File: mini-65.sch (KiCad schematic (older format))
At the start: 170 parts, among them J1 TYPE-C-31-M12_13_EDITED, J2 AVR-ISP-6, SW1 SW_Push, U1 ATmega32U4-AU, U2 USBLC6-2SC6, Y1 Crystal_GND24_Small

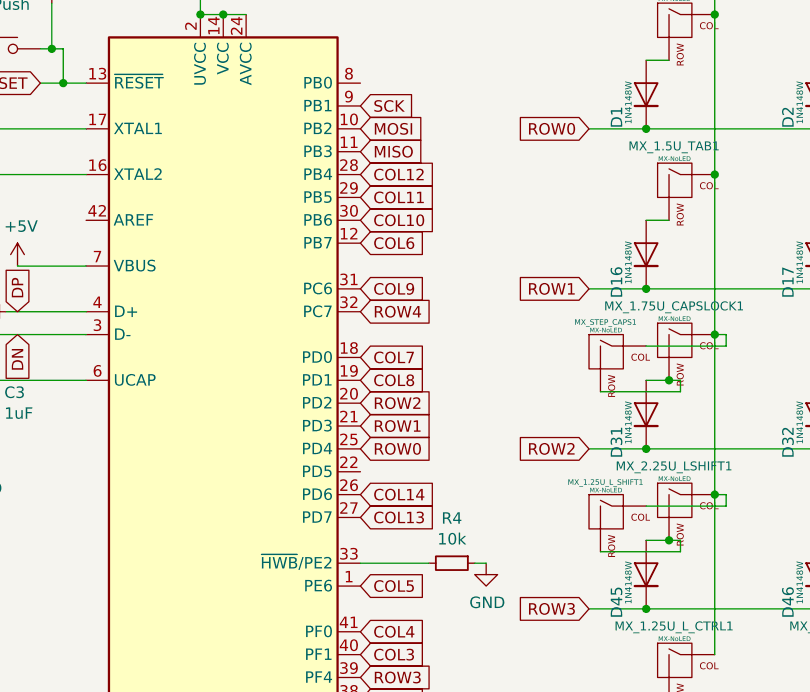
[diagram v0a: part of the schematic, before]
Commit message: All col/rows routed, ground screw pads extended
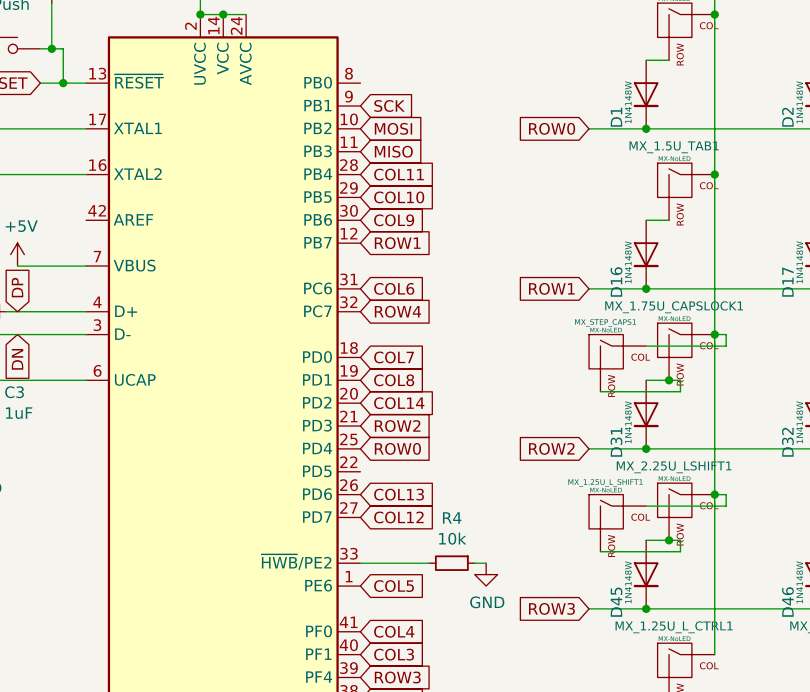
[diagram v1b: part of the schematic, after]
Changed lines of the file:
@@
 	1    0    0    -1
 $EndComp
-Text GLabel 3150 2950 2    50   Input ~ 0
-ROW0
-Text GLabel 3150 2850 2    50   Input ~ 0
-ROW1
-Text GLabel 3150 2750 2    50   Input ~ 0
-ROW2
 Wire Wire Line
 	2450 4650 2100 4650
@@
 	1    0    0    -1
 $EndComp
-Text GLabel 3150 3950 2    50   Input ~ 0
-ROW3
-Text GLabel 3150 2350 2    50   Input ~ 0
-ROW4
-Text GLabel 3150 4050 2    50   Input ~ 0
-COL0
-Text GLabel 3150 4150 2    50   Input ~ 0
-COL1
-Text GLabel 3150 4250 2    50   Input ~ 0
-COL2
-Text GLabel 3150 3850 2    50   Input ~ 0
-COL3
-Text GLabel 3150 3750 2    50   Input ~ 0
-COL4
-Text GLabel 3150 3550 2    50   Input ~ 0
-COL5
-Text GLabel 3150 2050 2    50   Input ~ 0
-COL6
-Text GLabel 3150 2550 2    50   Input ~ 0
-COL7
-Text GLabel 3150 2650 2    50   Input ~ 0
-COL8
-Text GLabel 3150 2250 2    50   Input ~ 0
-COL9
-Text GLabel 3150 1950 2    50   Input ~ 0
-COL10
-Text GLabel 3150 1850 2    50   Input ~ 0
-COL11
-Text GLabel 3150 1750 2    50   Input ~ 0
-COL12
-Text GLabel 3150 3150 2    50   Input ~ 0
-COL14
-Text GLabel 3150 3250 2    50   Input ~ 0
-COL13
 $Comp
 L Power_Protection:USBLC6-2SC6 U2
@@
 Wire Wire Line
 	8550 6350 8550 6400
+Text GLabel 3150 2950 2    50   Input ~ 0
+ROW0
+Text GLabel 3150 2050 2    50   Input ~ 0
+ROW1
+Text GLabel 3150 2850 2    50   Input ~ 0
+ROW2
+Text GLabel 3150 2750 2    50   Input ~ 0
+COL14
+Text GLabel 3150 3150 2    50   Input ~ 0
+COL13
+Text GLabel 3150 3250 2    50   Input ~ 0
+COL12
+Text GLabel 3150 1750 2    50   Input ~ 0
+COL11
+Text GLabel 3150 1850 2    50   Input ~ 0
+COL10
+Text GLabel 3150 1950 2    50   Input ~ 0
+COL9
+Text GLabel 3150 2650 2    50   Input ~ 0
+COL8
+Text GLabel 3150 2550 2    50   Input ~ 0
+COL7
+Text GLabel 3150 2250 2    50   Input ~ 0
+COL6
+Text GLabel 3150 3550 2    50   Input ~ 0
+COL5
+Text GLabel 3150 3750 2    50   Input ~ 0
+COL4
+Text GLabel 3150 3850 2    50   Input ~ 0
+COL3
+Text GLabel 3150 3950 2    50   Input ~ 0
+ROW3
+Text GLabel 3150 4050 2    50   Input ~ 0
+COL0
+Text GLabel 3150 4150 2    50   Input ~ 0
+COL1
+Text GLabel 3150 4250 2    50   Input ~ 0
+COL2
+Text GLabel 3150 2350 2    50   Input ~ 0
+ROW4
 $EndSCHEMATC

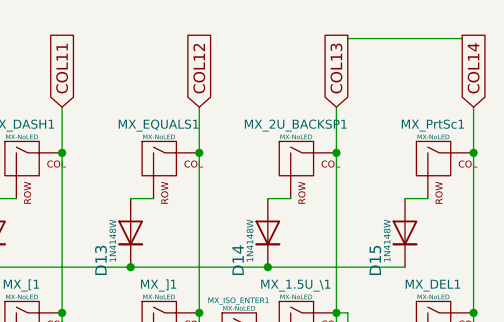
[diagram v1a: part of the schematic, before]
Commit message: Changed position of C5
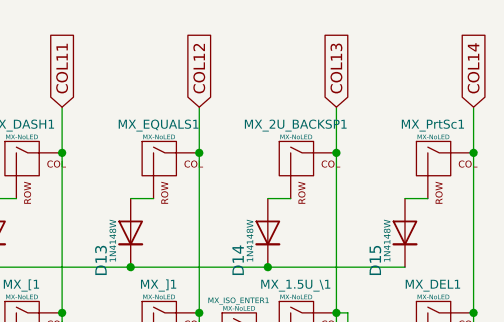
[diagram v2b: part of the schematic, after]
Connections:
- wire segments 325 -> 324
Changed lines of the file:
@@
 Connection ~ 12800 1050
-Wire Wire Line
-	12850 550  13350 550
 Wire Wire Line
 	11300 4350 11900 4350

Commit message: Changed diode positions and misc. ground changes
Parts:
- MX_6.25U_SPACE1: footprint MX_Only:MXOnly-6.25U-NoLED -> MX_Only:MXOnly-6.25U-ReversedStabilizers-NoLED
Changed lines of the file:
@@
 F 0 "MX_6.25U_SPACE1" H 8422 4074 39  0000 C CNN
 F 1 "MX-NoLED" H 8424 4019 20  0000 C CNN
-F 2 "MX_Only:MXOnly-6.25U-NoLED" H 7825 3875 60  0001 C CNN
+F 2 "MX_Only:MXOnly-6.25U-ReversedStabilizers-NoLED" H 7825 3875 60  0001 C CNN
 F 3 "" H 7825 3875 60  0001 C CNN
 	1    8450 3900

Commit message: Tweaked the MX footprints to include plated holes
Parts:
- MX_'1, MX_,1, MX_.1, MX_/1, MX_0, MX_1, MX_2, MX_3, MX_4, MX_5, MX_6, MX_7, MX_8, MX_9, MX_;1, MX_A1, MX_ARR_D1, MX_ARR_L1, MX_ARR_R1, MX_ARR_U1, MX_B1, MX_C1, MX_D1, MX_DASH1, MX_DEL1, MX_E1, MX_EQUALS1, MX_ESC1, MX_F1, MX_FN1, MX_G1, MX_H1, MX_I1, MX_INS1, MX_ISO_\1, MX_J1, MX_K1, MX_L1, MX_L_ALT1, MX_L_BSLASH1, MX_M1, MX_N1, MX_O1, MX_P1, MX_PrtSc1, MX_Q1, MX_R1, MX_R_CTRL1, MX_S1, MX_STEP_CAPS1, MX_T1, MX_TEMP1, MX_U1, MX_V1, MX_W1, MX_X1, MX_Y1, MX_Z1, MX_[1, MX_]1: footprint MX_Only:MXOnly-1U-NoLED -> mini-MX-Tweaks:MXOnly-1U-NoLED_tweak
- MX_1.25U_FN1, MX_1.25U_L_ALT1, MX_1.25U_L_CTRL1, MX_1.25U_L_SHIFT1, MX_1.25U_L_WIN1, MX_1.25U_R_CTRL1: footprint MX_Only:MXOnly-1.25U-NoLED -> mini-MX-Tweaks:MXOnly-1.25U-NoLED_tweak
- MX_1.5U_TAB1, MX_1.5U_\1: footprint MX_Only:MXOnly-1.5U-NoLED -> mini-MX-Tweaks:MXOnly-1.5U-NoLED_tweak
- MX_1.75U_CAPSLOCK1, MX_1.75U__RSHIFT1: footprint MX_Only:MXOnly-1.75U-NoLED -> mini-MX-Tweaks:MXOnly-1.75U-NoLED_tweak
- MX_2.25U_ENTER1, MX_2.25U_LSHIFT1: footprint MX_Only:MXOnly-2.25U-NoLED -> mini-MX-Tweaks:MXOnly-2.25U-NoLED_tweak
- MX_2U_BACKSP1: footprint MX_Only:MXOnly-2U-NoLED -> mini-MX-Tweaks:MXOnly-2U-NoLED_tweak
- MX_6.25U_SPACE1: footprint MX_Only:MXOnly-6.25U-ReversedStabilizers-NoLED -> mini-MX-Tweaks:MXOnly-6.25U-ReversedStabilizers-NoLED_tweak
- MX_ISO_ENTER1: footprint MX_Only:MXOnly-ISO-ROTATED-ReversedStabilizers-NoLED -> mini-MX-Tweaks:MXOnly-ISO-ROTATED-ReversedStabilizers-NoLED_tweak

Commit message: Updated PCB to tweaked footprints
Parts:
- D1, D10, D11, D12, D13, D14, D15, D16, D17, D18, D19, D2, D20, D21, D22, D23, D24, D25, D26, D27, D28, D29, D3, D30, D31, D32, D33, D34, D35, D36, D37, D38, D39, D4, D40, D41, D42, D43, D44, D45, D46, D47, D48, D49, D5, D50, D51, D52, D53, D54, D55, D56, D57, D58, D59, D6, D60, D61, D62, D63, D64, D65, D66, D67, D68, D69, D7, D8, D9: footprint canadian_footprints:D_SOD123_axial-dual -> mini-general-tweaks:D_SOD123_axial-dual
- H0, H1, H2, H3, H4, H5: footprint MountingHole:MountingHole_2.2mm_M2_Pad -> mini-general-tweaks:MountingHole_2.2mm_M2_Pad_tweaked
- J2: footprint Connector_PinHeader_2.54mm:PinHeader_2x03_P2.54mm_Vertical -> mini-general-tweaks:PinHeader_2x03_P2.54mm_Vertical_ICSP
- U1: footprint Package_QFP:TQFP-44_10x10mm_P0.8mm -> mini-general-tweaks:TQFP-44_10x10mm_P0.8mm_ATmega32U4
- U2: footprint Package_TO_SOT_SMD:SOT-23-6 -> mini-general-tweaks:SOT-23-6_tweaked

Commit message: Restructured USB area, general silkscreen tweaks
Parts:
- J1: footprint Type-C:HRO-TYPE-C-31-M-12-HandSoldering -> mini-general-tweaks:HRO-TYPE-C-31-M-12-HandSoldering_tweaked
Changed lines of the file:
@@
 F 0 "J1" H 4057 7867 50  0000 C CNN
 F 1 "TYPE-C-31-M12_13_EDITED" H 4057 7776 50  0000 C CNN
-F 2 "Type-C:HRO-TYPE-C-31-M-12-HandSoldering" V 3450 6500 50  0001 C CNN
+F 2 "mini-general-tweaks:HRO-TYPE-C-31-M-12-HandSoldering_tweaked" V 3450 6500 50  0001 C CNN
 F 3 "" H 4150 6500 50  0001 C CNN
 	1    3950 6450

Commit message: misc changes, including ICSP silkscreen
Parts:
- J2: footprint mini-general-tweaks:PinHeader_2x03_P2.54mm_Vertical_ICSP -> mini-general-tweaks:ICSP_2.54mm_LAYOUT
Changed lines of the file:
@@
 F 0 "J2" H 921 6596 50  0000 R CNN
 F 1 "AVR-ISP-6" H 921 6505 50  0000 R CNN
-F 2 "mini-general-tweaks:PinHeader_2x03_P2.54mm_Vertical_ICSP" V 950 6550 50  0001 C CNN
+F 2 "mini-general-tweaks:ICSP_2.54mm_LAYOUT" V 950 6550 50  0001 C CNN
 F 3 " ~" H -75 5950 50  0001 C CNN
 	1    1200 6500
@@
 	1    0    0    -1
 $EndComp
-Connection ~ 2450 1050
 Wire Wire Line
 	4200 2700 4550 2700
@@
 Wire Wire Line
 	8550 6350 8550 6400
-Text GLabel 3150 2950 2    50   Input ~ 0
-ROW0
-Text GLabel 3150 2050 2    50   Input ~ 0
-ROW1
-Text GLabel 3150 2850 2    50   Input ~ 0
-ROW2
-Text GLabel 3150 2750 2    50   Input ~ 0
-COL14
-Text GLabel 3150 3150 2    50   Input ~ 0
-COL13
-Text GLabel 3150 3250 2    50   Input ~ 0
-COL12
-Text GLabel 3150 1750 2    50   Input ~ 0
-COL11
-Text GLabel 3150 1850 2    50   Input ~ 0
-COL10
-Text GLabel 3150 1950 2    50   Input ~ 0
-COL9
-Text GLabel 3150 2650 2    50   Input ~ 0
-COL8
-Text GLabel 3150 2550 2    50   Input ~ 0
-COL7
-Text GLabel 3150 2250 2    50   Input ~ 0
-COL6
-Text GLabel 3150 2350 2    50   Input ~ 0
-ROW4
 Connection ~ 5450 3150
 Connection ~ 6500 3650
-Connection ~ 2550 1050
-Wire Wire Line
-	2650 1050 2550 1050
-Wire Wire Line
-	2550 1050 2450 1050
 Connection ~ 8300 4350
-Text GLabel 3150 4250 2    50   Input ~ 0
-COL2
-Text GLabel 3150 4150 2    50   Input ~ 0
-COL1
-Text GLabel 3150 4050 2    50   Input ~ 0
-COL0
-Text GLabel 3150 3950 2    50   Input ~ 0
-ROW3
-Text GLabel 3150 3850 2    50   Input ~ 0
-COL3
-Text GLabel 3150 3750 2    50   Input ~ 0
-COL4
-Text GLabel 3150 3550 2    50   Input ~ 0
-COL5
 Wire Wire Line
 	5450 3150 5450 3850
@@
 	5900 3650 6500 3650
 Connection ~ 4400 3650
-$Comp
-L MCU_Microchip_ATmega:ATmega32U4-AU U1
-U 1 1 5F16167A
-P 2550 2850
-F 0 "U1" H 2550 961 50  0000 C CNN
-F 1 "ATmega32U4-AU" H 2550 870 50  0000 C CNN
-F 2 "mini-general-tweaks:TQFP-44_10x10mm_P0.8mm_ATmega32U4" H 2550 2850 50  0001 C CIN
-F 3 "http://ww1.microchip.com/downloads/en/DeviceDoc/Atmel-7766-8-bit-AVR-ATmega16U4-32U4_Datasheet.pdf" H 2550 2850 50  0001 C CNN
-	1    2550 2850
-	1    0    0    -1
-$EndComp
 Wire Wire Line
 	3150 3450 3450 3450
-Connection ~ 2450 4650
-Wire Wire Line
-	2550 4650 2450 4650
-Wire Wire Line
-	2450 4650 2100 4650
 Connection ~ 5150 3650
 Wire Wire Line
@@
 	1    0    0    -1
 $EndComp
+Text GLabel 3150 3550 2    50   Input ~ 0
+COL5
+Text GLabel 3150 3750 2    50   Input ~ 0
+COL4
+Text GLabel 3150 3850 2    50   Input ~ 0
+COL3
+Text GLabel 3150 1850 2    50   Input ~ 0
+ROW3
+Text GLabel 3150 4050 2    50   Input ~ 0
+COL1
+Text GLabel 3150 4150 2    50   Input ~ 0
+COL0
+Text GLabel 3150 3950 2    50   Input ~ 0
+COL2
+Wire Wire Line
+	2450 4650 2100 4650
+Wire Wire Line
+	2550 4650 2450 4650
+Connection ~ 2450 4650
+Wire Wire Line
+	2550 1050 2450 1050
+Wire Wire Line
+	2650 1050 2550 1050
+Connection ~ 2550 1050
+Connection ~ 2450 1050
+Text GLabel 3150 4250 2    50   Input ~ 0
+ROW0
+Text GLabel 3150 2050 2    50   Input ~ 0
+ROW1
+Text GLabel 3150 1950 2    50   Input ~ 0
+ROW2
+Text GLabel 3150 2250 2    50   Input ~ 0
+COL14
+Text GLabel 3150 3250 2    50   Input ~ 0
+COL12
+Text GLabel 3150 3150 2    50   Input ~ 0
+COL11
+Text GLabel 3150 2950 2    50   Input ~ 0
+COL10
+Text GLabel 3150 2850 2    50   Input ~ 0
+COL9
+Text GLabel 3150 2750 2    50   Input ~ 0
+COL8
+Text GLabel 3150 2650 2    50   Input ~ 0
+COL7
+Text GLabel 3150 2550 2    50   Input ~ 0
+COL6
+Text GLabel 3150 2350 2    50   Input ~ 0
+ROW4
+$Comp
+L MCU_Microchip_ATmega:ATmega32U4-AU U1
+U 1 1 5F16167A
+P 2550 2850
+F 0 "U1" H 2550 961 50  0000 C CNN
+F 1 "ATmega32U4-AU" H 2550 870 50  0000 C CNN
+F 2 "mini-general-tweaks:TQFP-44_10x10mm_P0.8mm_ATmega32U4" H 2550 2850 50  0001 C CIN
+F 3 "http://ww1.microchip.com/downloads/en/DeviceDoc/Atmel-7766-8-bit-AVR-ATmega16U4-32U4_Datasheet.pdf" H 2550 2850 50  0001 C CNN
+	1    2550 2850
+	1    0    0    -1
+$EndComp
+Text GLabel 3150 1750 2    50   Input ~ 0
+COL13
 $EndSCHEMATC

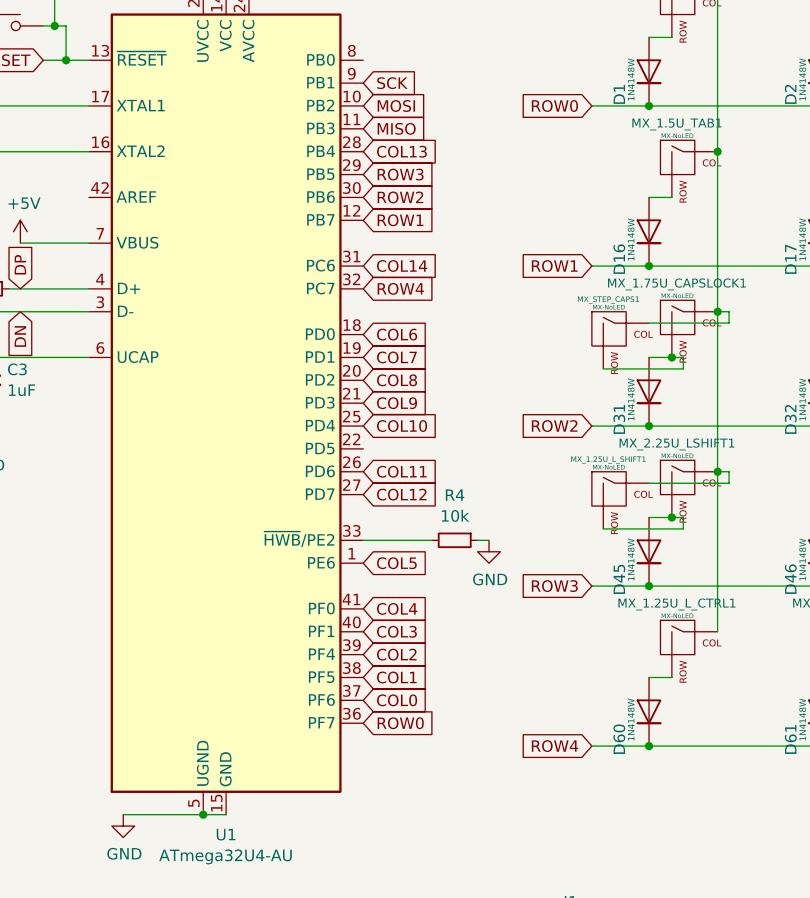
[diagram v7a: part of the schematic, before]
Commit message: misc traces edits, change some col/row linkings
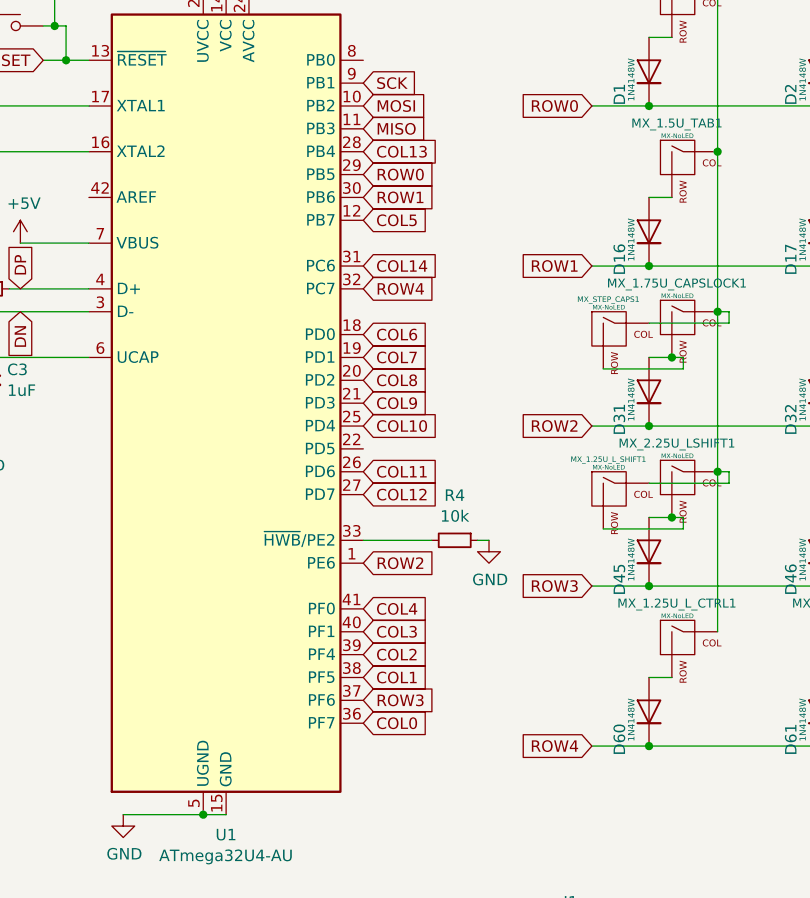
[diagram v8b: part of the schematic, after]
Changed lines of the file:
@@
 	1    0    0    -1
 $EndComp
-Text GLabel 3150 3550 2    50   Input ~ 0
+Text GLabel 3150 2050 2    50   Input ~ 0
 COL5
 Text GLabel 3150 3750 2    50   Input ~ 0
@@
 Text GLabel 3150 3850 2    50   Input ~ 0
 COL3
-Text GLabel 3150 1850 2    50   Input ~ 0
+Text GLabel 3150 4150 2    50   Input ~ 0
 ROW3
 Text GLabel 3150 4050 2    50   Input ~ 0
 COL1
-Text GLabel 3150 4150 2    50   Input ~ 0
+Text GLabel 3150 4250 2    50   Input ~ 0
 COL0
 Text GLabel 3150 3950 2    50   Input ~ 0
@@
 Connection ~ 2550 1050
 Connection ~ 2450 1050
-Text GLabel 3150 4250 2    50   Input ~ 0
+Text GLabel 3150 1850 2    50   Input ~ 0
 ROW0
-Text GLabel 3150 2050 2    50   Input ~ 0
+Text GLabel 3150 1950 2    50   Input ~ 0
 ROW1
-Text GLabel 3150 1950 2    50   Input ~ 0
+Text GLabel 3150 3550 2    50   Input ~ 0
 ROW2
 Text GLabel 3150 2250 2    50   Input ~ 0
